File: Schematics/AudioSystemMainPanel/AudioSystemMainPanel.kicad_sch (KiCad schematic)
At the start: 30 parts, among them J1 AudioJack3, J2 AudioJack3, U1 DEVKIT_V1_ESP32-WROOM-32, U2 PCM5102A, U3 OPA2134, U4 OPA2134

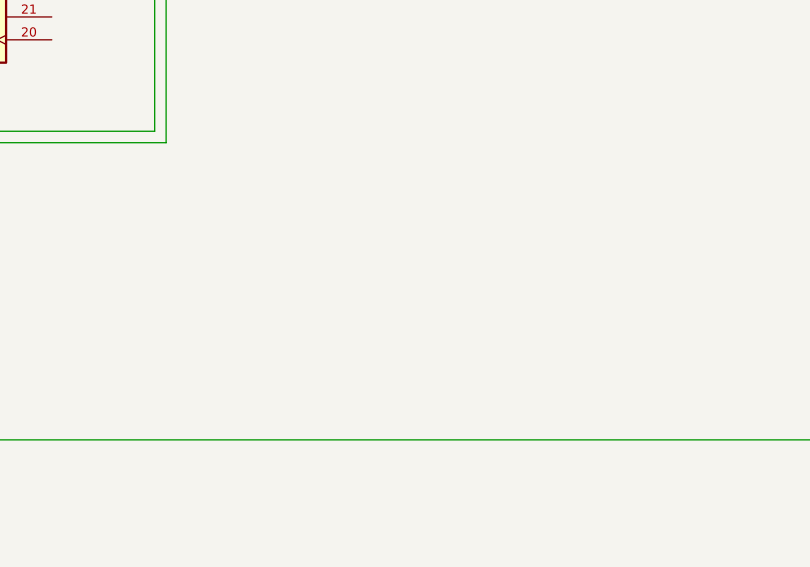
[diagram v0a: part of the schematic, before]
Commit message: added full audio system schematic (not completed)
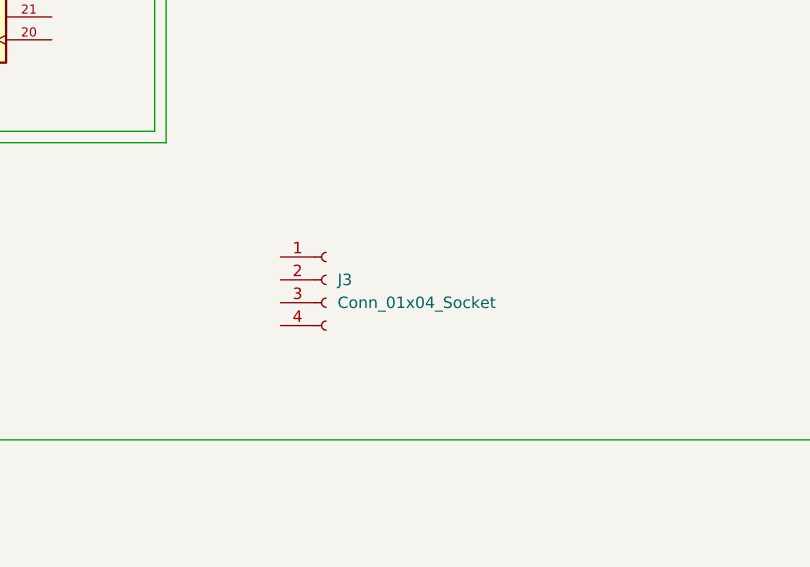
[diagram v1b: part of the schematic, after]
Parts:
- added J3: Conn_01x04_Socket, symbol Connector:Conn_01x04_Socket
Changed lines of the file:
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@@
+	)
+	(symbol
+		(lib_id "Connector:Conn_01x04_Socket")
+		(at 190.5 110.49 0)
+		(unit 1)
+		(exclude_from_sim no)
+		(in_bom yes)
+		(on_board yes)
+		(dnp no)
+		(fields_autoplaced yes)
+		(property "Reference" "J3"
+			(at 191.77 110.4899 0)
+			(effects
+				(font
+					(size 1.27 1.27)
+				)
+				(justify left)
+			)
+		)
+		(property "Value" "Conn_01x04_Socket"
+			(at 191.77 113.0299 0)
+			(effects
+				(font
+					(size 1.27 1.27)
+				)
+				(justify left)
+			)
+		)
+		(property "Footprint" ""
+			(at 190.5 110.49 0)
+			(effects
+				(font
+					(size 1.27 1.27)
+				)
+				(hide yes)
+			)
+		)
+		(property "Datasheet" "~"
+			(at 190.5 110.49 0)
+			(effects
+				(font
+					(size 1.27 1.27)
+				)
+				(hide yes)
+			)
+		)
+		(property "Description" "Generic connector, single row, 01x04, script generated"
+			(at 190.5 110.49 0)
+			(effects
+				(font
+					(size 1.27 1.27)
+				)
+				(hide yes)
+			)
+		)
+		(pin "3"
+		)
+		(pin "4"
+		)
+		(pin "1"
+		)
+		(pin "2"
+		)
+		(instances
+			(project ""
+				(path "/ff53e594-6401-4e7d-9332-9d87eb1f5f5d"
+					(reference "J3")
+					(unit 1)
+				)
+			)
+		)
 	)
 	(symbol
